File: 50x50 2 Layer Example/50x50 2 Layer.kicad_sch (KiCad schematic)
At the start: 64 parts, among them J1 USB_C_Receptacle_USB2.0_14P, J2 Conn_01x02, J3 Conn_01x03, J5 Conn_01x02, J6 Conn_01x04, SW1 Reset, SW2 SW_SPST, U1 RP2040, U2 W25Q128JVPIQ TR, U4 Voltage Regulator, U5 DMG2305UX-7, Y1 12MHz

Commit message: Updated Schematic
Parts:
- removed U5: DMG2305UX-7, SOT-23_DIO, symbol 2024-04-02_02-23-06:DMG2305UX-7
- added Q1: DMG2305UX-7, DMG2305UX-7:SOT-23_DIO, symbol Simulation_SPICE:PMOS
- added R1: 0R, symbol Device:R
- added R2: 10K, Resistor_SMD:R_0805_2012Metric_Pad1.20x1.40mm_HandSolder, symbol Device:R
- F1: value 3A -> 0.15A
- R7: renamed from R17; value 360R -> 470R
- renumbered C6 to C10, C7 to C11, C8 to C12, C9 to C13, C10 to C14, C11 to C15, C12 to C16, C13 to C2, C14 to C3, C2 to C4, C3 to C5, C15 to C6, C16 to C7, C4 to C8, C5 to C9, D5 to D1, D6 to D2, D7 to D3, D1 to D5, D2 to D6, D3 to D7, H4 to H2, H2 to H3, H3 to H4, J5 to J1, J1 to J3, J3 to J4, J6 to J5, R6 to R10, R5 to R11, R16 to R12, R19 to R13, R18 to R14, R7 to R15, R8 to R16, R9 to R17, R10 to R18, R13 to R19, R14 to R20, R15 to R21, R11 to R5, R1 to R6, R2 to R8, R12 to R9, SW2 to SW1, SW1 to SW2, TP3 to TP1, TP4 to TP2, TP2 to TP3, TP1 to TP4, U2 to U1, U4 to U2, U1 to U3, U3 to U4
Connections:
- net Batt: now also F1.2
- net GND: now also R1.2, R2.2; no longer J3.S1 (SHIELD)
- net VBUS: now also Q1.2 (G), R2.1
- net VBatt renamed +BATT
- net +BATT: now also Q1.3 (S); no longer SW1.2 (B)
- new net: J3.S1 (SHIELD), R1.1
- new net: Q1.1 (D), SW1.2 (B)
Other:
- note added: "3V3 Regulator"
- note added: "Bypass and decoupling capacitors"
- note added: "Crystal"
- note added: "Debug Port"
- note added: "Flash"
- note added: "I2C Pullups"
- note added: "Internal 1.1v regulator bypass"
- note added: "Mounting holes"
- note added: "RP2040"
- note added: "Reset Button"
- note added: "Sensors and screen"
- note added: "Status LEDs"
- note added: "USB C"
- note removed: "3V3 Voltage Regulator"
- moved on the sheet: C1, C10, C11, C12, C13, C14, C15, C16, C2, C3, C4, C5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

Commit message: Updated board and schematic
PCB and schematic have been updated to REV B
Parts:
- removed Q1: DMG2305UX-7, DMG2305UX-7:SOT-23_DIO, symbol Simulation_SPICE:PMOS
- removed R2: 10K, Resistor_SMD:R_0805_2012Metric_Pad1.20x1.40mm_HandSolder, symbol Device:R
- added D2: D_Schottky, Diode_SMD:D_SMA, symbol Device:D_Schottky
- added TP11: INT_1, TestPoint:TestPoint_Pad_1.0x1.0mm, symbol Connector:TestPoint
- added TP12: I2C0_SCL, TestPoint:TestPoint_Pad_1.0x1.0mm, symbol Connector:TestPoint
- added TP13: I2C1_SCL, TestPoint:TestPoint_Pad_1.0x1.0mm, symbol Connector:TestPoint
- added TP14: I2C0_SDA, TestPoint:TestPoint_Pad_1.0x1.0mm, symbol Connector:TestPoint
- added TP15: I2C1_SDA, TestPoint:TestPoint_Pad_1.0x1.0mm, symbol Connector:TestPoint
- added TP3: D-, TestPoint:TestPoint_Pad_1.0x1.0mm, symbol Connector:TestPoint
- added TP4: D+, TestPoint:TestPoint_Pad_1.0x1.0mm, symbol Connector:TestPoint
- added TP5: USB_BOOT, TestPoint:TestPoint_Pad_1.0x1.0mm, symbol Connector:TestPoint
- added TP6: USB_DET, TestPoint:TestPoint_Pad_1.0x1.0mm, symbol Connector:TestPoint
- added TP7: BATT, TestPoint:TestPoint_Pad_1.0x1.0mm, symbol Connector:TestPoint
- added TP9: RST, TestPoint:TestPoint_Pad_1.0x1.0mm, symbol Connector:TestPoint
- C15: value 1uF -> 100nF
- R1: footprint (none) -> Resistor_SMD:R_0805_2012Metric_Pad1.20x1.40mm_HandSolder
- TP1: value TestPoint -> GND
- TP2: value TestPoint -> VBUS
- TP8: renamed from TP3; value TestPoint -> 3V3
- U4: footprint Sense Board:SenseBoard -> Sense Board:UCA_Sense
- renumbered D2 to D3, D3 to D4, D4 to D5, D5 to D6, D6 to D7, D7 to D8, R11 to R10, R12 to R11, R13 to R12, R14 to R13, R15 to R14, R16 to R15, R17 to R16, R18 to R17, R19 to R18, R20 to R19, R3 to R2, R21 to R20, R4 to R3, R5 to R4, R6 to R5, R7 to R6, R8 to R7, R9 to R8, R10 to R9, TP4 to TP10, U3 to U1, U1 to U2, U2 to U3
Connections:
- net GPIO_8 is gone; now on net INT_1: U1.11 (GPIO8)
- net +3V3: now also U4.6 (+3V3); no longer U4.1 (VIN)
- net +BATT: now also D2.1 (K), TP7.1; no longer TP2.1
- net D+: now also TP4.1
- net D-: now also TP3.1
- net GND: now also U4.4 (GND); no longer U4.3 (GND)
- net I2C0_SCL: now also TP12.1
- net I2C0_SDA: now also TP14.1
- net I2C1_SCL: now also U4.1 (SCL), TP13.1; no longer U4.4 (SCL)
- net I2C1_SDA: now also U4.3 (SDA), TP15.1; no longer U4.6 (SDA)
- net QSPI_SS: now also TP5.1
- net RUN: now also TP9.1
- net USB_DET: now also TP6.1
- net VBUS: now also TP2.1
- net INT_1: now reaches U4.2 (INT_1)
- net INT_1: now also TP11.1
- net at SW1.2 (B): now also D2.2 (A)
- net Batt renamed Battery
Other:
- title: Tutorial Board -> Avionics Tutorial Example Board
- moved on the sheet: C4, C5, D1, D3, D4, R9, Y1

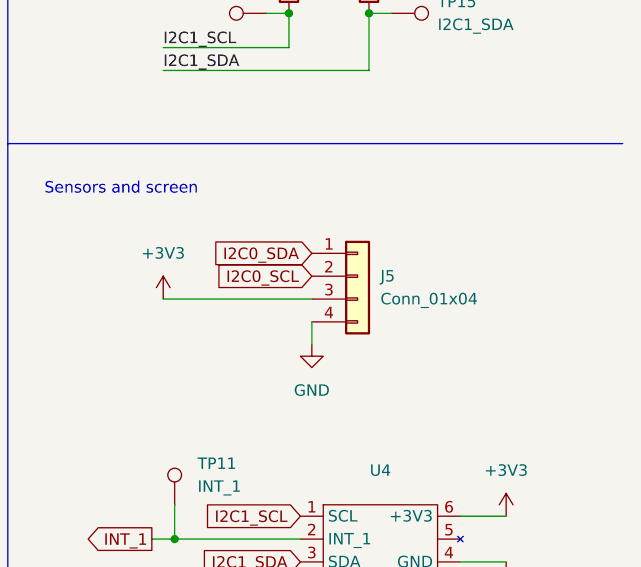
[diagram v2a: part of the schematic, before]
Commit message: Fixed screen connector and tidied GND plane
The OLED screen connector was flipped, so fixed that. Tidied up some long GND paths as well.
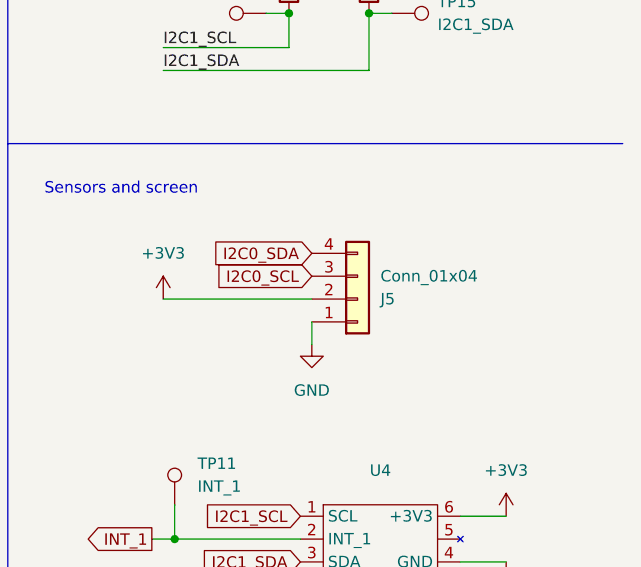
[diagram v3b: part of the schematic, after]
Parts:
- J2: footprint Connector_PinSocket_2.54mm:PinSocket_1x02_P2.54mm_Vertical -> Connector_PinHeader_2.54mm:PinHeader_1x02_P2.54mm_Vertical
- J5: footprint Connector_PinHeader_2.54mm:PinHeader_1x04_P2.54mm_Vertical -> Connector_PinSocket_2.54mm:PinSocket_1x04_P2.54mm_Vertical
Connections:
- net +3V3: now also J5.2 (Pin_2); no longer J5.3 (Pin_3)
- net GND: now also J5.1 (Pin_1); no longer J5.4 (Pin_4)
- net I2C0_SCL: now also J5.3 (Pin_3); no longer J5.2 (Pin_2)
- net I2C0_SDA: now also J5.4 (Pin_4); no longer J5.1 (Pin_1)
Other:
- title: Avionics Tutorial Example Board -> Avionics Tutorial 50x50mm Example Board
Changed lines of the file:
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@@
 	(paper "A3")
 	(title_block
-		(title "Avionics Tutorial Example Board")
+		(title "Avionics Tutorial 50x50mm Example Board")
 		(date "2024-04-12")
 		(rev "B")
@@
 	(wire
 		(pts
-			(xy 356.87 160.02) (xy 373.38 160.02)
-		)
-		(stroke
-			(width 0)
-			(type default)
-		)
-	)
-	(wire
-		(pts
 			(xy 389.89 31.75) (xy 389.89 43.18)
 		)
@@
 	(wire
 		(pts
+			(xy 356.87 160.02) (xy 373.38 160.02)
+		)
+		(stroke
+			(width 0)
+			(type default)
+		)
+	)
+	(wire
+		(pts
 			(xy 238.76 137.16) (xy 248.92 137.16)
 		)
@@
 			)
 		)
-		(property "Footprint" "Connector_PinSocket_2.54mm:PinSocket_1x02_P2.54mm_Vertical"
+		(property "Footprint" "Connector_PinHeader_2.54mm:PinHeader_1x02_P2.54mm_Vertical"
 			(at 39.37 138.43 0)
 			(effects
@@
 	(symbol
 		(lib_id "Connector_Generic:Conn_01x04")
-		(at 378.46 157.48 0)
+		(at 378.46 160.02 0)
+		(mirror x)
 		(unit 1)
 		(exclude_from_sim no)
@@
 		(on_board yes)
 		(dnp no)
-		(fields_autoplaced yes)
 		(property "Reference" "J5"
-			(at 381 157.4799 0)
+			(at 381 160.0201 0)
 			(effects
 				(font
@@
 		)
 		(property "Value" "Conn_01x04"
-			(at 381 160.0199 0)
+			(at 381 157.4801 0)
 			(effects
 				(font
@@
 			)
 		)
-		(property "Footprint" "Connector_PinHeader_2.54mm:PinHeader_1x04_P2.54mm_Vertical"
-			(at 378.46 157.48 0)
+		(property "Footprint" "Connector_PinSocket_2.54mm:PinSocket_1x04_P2.54mm_Vertical"
+			(at 378.46 160.02 0)
 			(effects
 				(font
@@
 		)
 		(property "Datasheet" "~"
-			(at 378.46 157.48 0)
+			(at 378.46 160.02 0)
 			(effects
 				(font
@@
 		)
 		(property "Description" "Generic connector, single row, 01x04, script generated (kicad-library-utils/schlib/autogen/connector/)"
-			(at 378.46 157.48 0)
+			(at 378.46 160.02 0)
 			(effects
 				(font
